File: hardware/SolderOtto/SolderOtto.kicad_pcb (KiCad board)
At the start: 4 copper layers, 121 x 60 mm, 221 parts, among them J201 Conn_02x04_Counter_Clockwise, J301 TC-2050, J401 Conn_01x20, J501 Conn_01x08, J601 Conn_01x07, P301 USB_C_Plug_USB2.0, Q201 T2N7002AK, Q202 BC858B, Q203 BC847A, Q204 BC847A, Q801 Q_Dual_NMOS, Q802 Q_Dual_NMOS, Q803 Q_Dual_NMOS, Q804 DTD123EK, Q805 DTD123EK, Q806 DTD123EK, Q807 Q_Dual_NMOS, Q808 Q_Dual_NMOS, Q809 DTD123EK, Q810 DTD123EK, Q901 BC847A, Q902 BC858B, Q903 BC847A, SW301 SW_Push, U201 LM5012, U202 AP3211K, U203 AP3211K, U204 AP3211K, U205 LM27761, U206 MCP9701T-E/TT, U301 USBLC6-2SC6, U302 STM32G474QETx, U303 MX25R3235FM1xx0, U701 SN74LVC125A, U702 TS5A3159ADCK, U801 VOM1271, U802 VOM1271, U803 VOM1271, U804 VOM1271, U805 VOM1271, U901 OP07, U902 LM358, U903 74hc4053, U904 OP07, U905 OP07, Y301 32.768 kHz

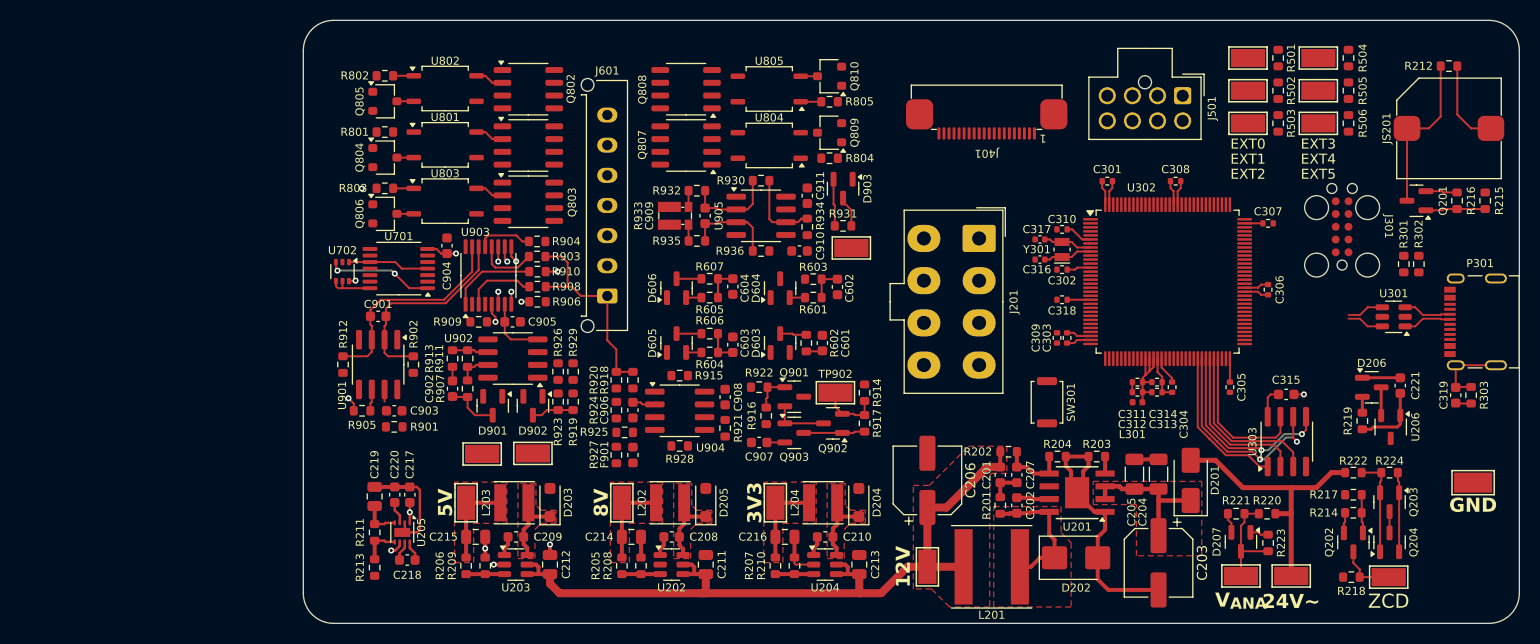
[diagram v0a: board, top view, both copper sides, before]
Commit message: try to replace op07c
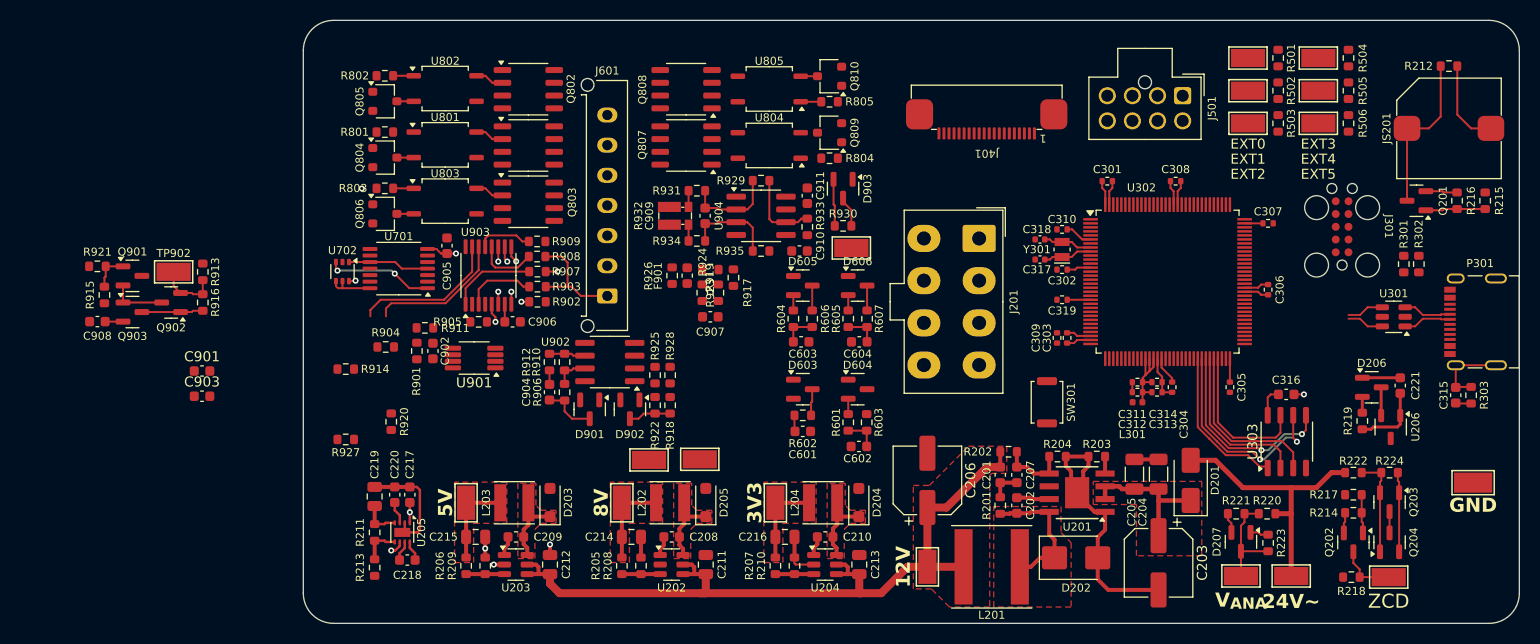
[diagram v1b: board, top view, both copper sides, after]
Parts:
- removed the C908 at (151.0, 87.5)
- removed the R901 at (118.0, 90.5)
- removed the U904 at (146.4, 88.8)
- added C901: 100n, Capacitor_SMD:C_0603_1608Metric, F.Cu at (98.9, 84.9)
- C903: value 1u -> 100n
- U303: footprint Package_SO:SOIC-8_3.9x4.9mm_P1.27mm -> Package_SO:SOP-8_3.9x4.9mm_P1.27mm
- U901: value OP07 -> OPA2206; footprint Package_SO:SOIC-8_3.9x4.9mm_P1.27mm -> Package_SO:VSSOP-8_3x3mm_P0.65mm
- moved C908 66.9 mm to (88.5, 80.0)
- moved R921 66.9 mm to (88.5, 74.5)
- moved Q901 66.9 mm to (92.0, 75.4)
- moved Q902 66.9 mm to (95.8, 78.1)
- moved Q903 66.9 mm to (92.0, 79.0)
- moved R913 66.9 mm to (99.0, 75.0)
- moved R915 66.9 mm to (89.2, 77.3)
- moved R916 66.9 mm to (99.0, 78.1)
- moved TP902 66.9 mm to (96.1, 75.0)
- moved R914 33.2 mm to (113.2, 84.7)
- moved R920 33.2 mm to (117.8, 89.9)
- moved R927 33.2 mm to (113.2, 91.7)
- moved C903 19.2 mm to (98.9, 87.4)
- moved R926 18.7 mm to (145.7, 75.4), turned to 90 degrees
- moved F901 18.6 mm to (147.2, 75.4), turned to 90 degrees
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- renumbered C319 to C315, C315 to C316, C316 to C317, C317 to C318, C318 to C319, C901 to C902, C902 to C904, C904 to C905, C905 to C906, C906 to C907, C907 to C908, R902 to R901, R906 to R902, R908 to R903, R905 to R904, R909 to R905, R907 to R906, R910 to R907, R903 to R908, R904 to R909, R911 to R910, R912 to R911, R913 to R912, R914 to R913, R915 to R914, R916 to R915, R917 to R916, R918 to R917, R919 to R918, R920 to R919, R921 to R920, R922 to R921, R923 to R922, R924 to R923, R925 to R924, R926 to R925, R927 to R926, R928 to R927, R929 to R928, R930 to R929, R931 to R930, R932 to R931, R933 to R932, R934 to R933, R935 to R934, R936 to R935, U905 to U904
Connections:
- C902 pad 2: Net-(U901-+) -> Net-(U901B-+)
- C903 pad 1: +8V -> -5V
- C907 pad 1: Net-(U904--) (its old number) -> Net-(U901A--)
- C907 pad 2: Net-(U904-+) (its old number) -> Net-(U901A-+)
- R901 pad 2: Net-(R902-Pad2) -> Net-(R901-Pad2)
- R904 pad 1: Net-(R902-Pad2) -> Net-(R901-Pad2)
- R911 pad 1: Net-(U901-+) -> Net-(U901B-+)
- R914 pad 1: Net-(U904--) (its old number) -> Net-(U901A--)
- R914 pad 2: Net-(R915-Pad2) -> Net-(R914-Pad2)
- R917 pad 2: Net-(U904--) (its old number) -> Net-(U901A--)
- R920 pad 1: Net-(R915-Pad2) -> Net-(R914-Pad2)
- R924 pad 1: Net-(U904-+) (its old number) -> Net-(U901A-+)
- R927 pad 1: Net-(U904-+) (its old number) -> Net-(U901A-+)
- U901 pad 1: unconnected-(U901-VOS-Pad1) -> Net-(R914-Pad2)
- U901 pad 2: /Channel0/channel_meas/IN- -> Net-(U901A--)
- U901 pad 3: Net-(U901-+) -> Net-(U901A-+)
- U901 pad 5: unconnected-(U901-NC-Pad5) -> Net-(U901B-+)
- U901 pad 6: Net-(R902-Pad2) -> /Channel0/channel_meas/IN-
- U901 pad 7: +8V -> Net-(R901-Pad2)
- U901 pad 8: Net-(R901-Pad2) -> +8V
- U903 pad 15: Net-(U901-+) -> Net-(U901B-+)
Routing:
- net Net-(U901-+): track 22.3 -> 0.00 mm
- net Net-(U901B-+): track 0.00 -> 15.7 mm
- net /Channel0/TC: track 20.9 -> 11.4 mm
- net /Channel0/channel_meas/IN-: track 20.6 -> 13.9 mm
- net -5V: track 10.3 -> 5.60 mm
- net Net-(U904--) (its old number): track 2.26 -> 0.00 mm
- net Net-(R902-Pad2): track 2.18 -> 0.00 mm
- net Net-(U902B-+): track 1.47 -> 0.00 mm, vias 1 -> 0
- net +8V: track 10.1 -> 8.85 mm

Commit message: save work
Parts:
- removed C911: 1u, Capacitor_SMD:C_0603_1608Metric
- removed U904: OP07, Package_SO:SOIC-8_3.9x4.9mm_P1.27mm
- added C912: 100n, Capacitor_SMD:C_0603_1608Metric, F.Cu at (128.0, 87.6)
- added C913: 100n, Capacitor_SMD:C_0603_1608Metric, F.Cu at (154.4, 66.8)
- added U905: OPA206, Package_SO:VSSOP-8_3x3mm_P0.65mm, F.Cu at (153.4, 69.5)
- U902: value LM358 -> LM358B; footprint Package_SO:SOIC-8_3.9x4.9mm_P1.27mm -> Package_SO:VSSOP-8_3x3mm_P0.65mm
- moved R917 62.5 mm to (88.6, 87.2)
- moved R919 62.5 mm to (90.1, 85.7)
- moved C907 62.5 mm to (87.8, 89.6)
- moved R923 62.5 mm to (87.8, 84.9)
- moved R924 62.5 mm to (87.0, 87.2)
- moved F901 62.5 mm to (85.5, 85.5)
- moved R926 62.5 mm to (84.0, 85.5)
- moved C903 57.6 mm to (154.4, 72.1)
- moved TP901 55.8 mm to (88.2, 101.6)
- moved TP903 49.1 mm to (100.0, 101.6)
- moved C904 46.8 mm to (88.0, 98.0)
- moved R906 46.8 mm to (89.5, 98.0)
- moved R910 46.8 mm to (89.5, 95.0)
- moved R912 46.8 mm to (88.0, 95.0)
- moved U902 46.8 mm to (94.0, 95.0)
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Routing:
- net Net-(U905-+): track 9.07 -> 0.00 mm
- net Net-(U905--): track 9.07 -> 0.00 mm
- net Net-(R929-Pad2): track 7.88 -> 0.00 mm
- net +3V3: track 53.4 -> 48.7 mm
- net Net-(U902A--): track 0.00 -> 4.09 mm
- net Net-(R922-Pad2): track 0.00 -> 3.94 mm
- net /Channel0/T_{TIP}: track 5.40 -> 1.52 mm
- net /Channel0/I_{LOAD}: track 3.10 -> 0.00 mm
- net Net-(R932-Pad3): track 1.62 -> 0.00 mm
- net Net-(R931-Pad1): track 1.61 -> 0.00 mm
- net Net-(U902B--): track 3.60 -> 2.59 mm

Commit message: save work
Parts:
- removed the R919 at (90.1, 85.7)
- added C904: 100n, Capacitor_SMD:C_0603_1608Metric, F.Cu at (120.8, 87.2)
- added C907: 100n, Capacitor_SMD:C_0603_1608Metric, F.Cu at (103.5, 92.3)
- added C910: 1n, Capacitor_SMD:C_0603_1608Metric, F.Cu at (104.5, 82.5)
- added U904: OPA202, Package_SO:VSSOP-8_3x3mm_P0.65mm, F.Cu at (102.0, 95.0)
- R923: value 220m -> 400m; footprint Resistor_SMD:R_0603_1608Metric -> Resistor_SMD:R_1206_3216Metric
- U901: value OPA2206 -> OPA202
- U905: value OPA206 -> OPA202
- moved TP903 46.4 mm to (145.2, 91.3)
- moved R919 46.3 mm to (145.2, 88.4)
- moved R922 46.3 mm to (143.7, 88.4)
- moved R925 46.3 mm to (143.7, 85.4)
- moved R928 46.3 mm to (145.2, 85.4)
- moved D901 46.2 mm to (137.3, 89.1)
- moved D902 46.2 mm to (141.1, 89.1)
- moved C903 46.2 mm to (133.2, 88.4)
- moved R906 46.2 mm to (134.7, 88.4)
- moved R910 46.2 mm to (134.7, 85.4)
- moved R912 46.2 mm to (133.2, 85.4)
- moved U902 46.2 mm to (139.2, 85.4)
- moved TP901 46.2 mm to (133.2, 91.3)
- moved C911 27.2 mm to (102.8, 97.7), turned to 0 degrees
- moved C901 26.6 mm to (124.7, 91.3)
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- renumbered C904 to C903, C907 to C909, C912 to C911, C913 to C912, C909 to C913, C910 to C914, C903 to C915, R915 to R914, R916 to R915, R914 to R916, R921 to R918, R918 to R919, R920 to R921
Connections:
- C902 pad 2: Net-(U901B-+) -> Net-(U901A-+)
- C909 pad 1: Net-(U901A--) -> Net-(U904A--)
- C909 pad 2: Net-(U901A-+) -> Net-(U904A-+)
- R911 pad 1: Net-(U901B-+) -> Net-(U901A-+)
- R916 pad 1: Net-(U901A--) -> Net-(U904A--)
- R916 pad 2: Net-(R914-Pad2) -> Net-(R916-Pad2)
- R917 pad 2: Net-(U901A--) -> Net-(U904A--)
- R921 pad 1: Net-(R914-Pad2) -> Net-(R916-Pad2)
- R923 pad 1: Net-(R919-Pad2) -> /Channel0/TC
- R924 pad 1: Net-(U901A-+) -> Net-(U904A-+)
- R927 pad 1: Net-(U901A-+) -> Net-(U904A-+)
- U901 pad 1: Net-(R914-Pad2) -> unconnected-(U901A-NC-Pad1)
- U901 pad 2: Net-(U901A--) -> /Channel0/channel_meas/IN-
- U901 pad 5: Net-(U901B-+) -> unconnected-(U901A-NC-Pad5)
- U901 pad 6: /Channel0/channel_meas/IN- -> Net-(R901-Pad2)
- U901 pad 7: Net-(R901-Pad2) -> +8V
- U901 pad 8: +8V -> unconnected-(U901A-NC-Pad8)
- U903 pad 15: Net-(U901B-+) -> Net-(U901A-+)
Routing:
- net Net-(U901B-+): track 15.7 -> 0.00 mm
- net /Channel0/channel_meas/IN-: track 13.9 -> 4.11 mm
- net Net-(R929-Pad2): track 0.00 -> 9.41 mm
- net Net-(U903-2Y1): track 8.61 -> 0.00 mm
- net /Channel0/I_{LOAD}: track 0.00 -> 8.11 mm
- net Net-(U903-3Y1): track 7.13 -> 0.00 mm
- net Net-(U903-1Y0): track 6.02 -> 0.00 mm
- net Net-(R901-Pad2): track 0.00 -> 5.89 mm
- net Net-(U903-1Y1): track 5.54 -> 0.00 mm
- net GND: track 94.8 -> 89.2 mm, vias 7 -> 4
- net Net-(U905A-+): track 0.00 -> 5.51 mm
- net Net-(U905A--): track 0.00 -> 5.46 mm
- net /Channel0/T_{TIP}: track 1.52 -> 6.58 mm
- net Net-(U901A-+): track 0.00 -> 4.11 mm
- net Net-(U902A-+): track 0.00 -> 3.81 mm
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
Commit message: save work
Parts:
- added R919: 220m, Resistor_SMD:R_0805_2012Metric, F.Cu at (148.9, 75.7)
- R923: value 400m -> 220m; footprint Resistor_SMD:R_1206_3216Metric -> Resistor_SMD:R_0805_2012Metric
- moved R917 59.6 mm to (153.3, 75.8), turned to 0 degrees
- moved R916 57.2 mm to (154.2, 78.3), turned to -90 degrees
- moved C909 56.5 mm to (151.6, 77.5), turned to 180 degrees
- moved R924 55.2 mm to (148.1, 77.5), turned to 180 degrees
- moved R926 54.9 mm to (145.9, 78.3)
- moved R923 54.4 mm to (145.3, 75.7), turned to 180 degrees
- moved F901 52.2 mm to (144.4, 78.2)
- moved C907 51.6 mm to (154.2, 83.2), turned to -90 degrees
- moved U904 51.4 mm to (151.6, 81.5), turned to -90 degrees
- moved C911 48.9 mm to (148.9, 81.5), turned to -90 degrees
- moved C910 39.2 mm to (143.3, 87.8), turned to 90 degrees
- moved R927 36.0 mm to (148.1, 79.0), turned to 180 degrees
- moved C908 30.3 mm to (116.9, 90.5), turned to -90 degrees
- moved R914 28.0 mm to (114.2, 89.8), turned to 180 degrees
- moved R918 28.0 mm to (111.4, 90.5), turned to 90 degrees
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- renumbered R919 to R920
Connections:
- R923 pad 1: /Channel0/TC -> Net-(R919-Pad2)
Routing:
- net /Channel0/channel_meas/IN-: track 4.11 -> 16.6 mm
- net Net-(U901A-+): track 4.11 -> 16.6 mm
- net /Channel0/TC: track 11.4 -> 0.00 mm
- net +8V: track 12.4 -> 15.9 mm
- net -5V: track 8.12 -> 11.0 mm
- net Net-(R901-Pad2): track 5.89 -> 7.95 mm
- net Net-(U902A--): track 2.86 -> 4.36 mm
- net GND: track 89.2 -> 90.6 mm
- net /Channel0/LOAD: track 1.18 -> 0.00 mm, vias 1 -> 0
- net /Channel0/I_{LEAK}: track 6.51 -> 5.98 mm
- net Net-(U903-3Y0): vias 1 -> 0

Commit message: save work
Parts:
- moved D605 14.3 mm to (144.8, 79.8), turned to 90 degrees
- moved C602 13.7 mm to (160.7, 75.2)
- moved D604 13.7 mm to (155.0, 75.3)
- moved R601 13.7 mm to (158.3, 76.2)
- moved R603 13.7 mm to (158.3, 74.4)
- moved C601 13.6 mm to (149.0, 75.4)
- moved D603 13.6 mm to (144.8, 75.4)
- moved R602 13.6 mm to (147.4, 75.4)
- moved R606 11.6 mm to (148.1, 78.9), turned to 0 degrees
- moved R916 10.2 mm to (160.3, 86.4)
- moved R926 10.2 mm to (152.1, 86.4)
- moved R927 10.2 mm to (154.3, 87.2)
- moved C907 10.2 mm to (160.4, 91.3)
- moved C909 10.2 mm to (157.8, 85.6)
- moved F901 10.2 mm to (150.6, 86.3)
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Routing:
- net Net-(U901A-+): track 16.6 -> 11.8 mm
- net /Channel0/channel_meas/IN-: track 16.6 -> 11.8 mm
- net Net-(R901-Pad2): track 7.95 -> 7.05 mm

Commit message: save work
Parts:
- moved J501 5.48 mm to (192.5, 53.8), turned to 0 degrees
- moved J201 2.30 mm to (176.2, 74.0)
- moved TP501 2.06 mm to (201.0, 54.2)
- moved TP502 2.06 mm to (201.0, 57.5)
- moved TP503 2.06 mm to (201.0, 60.8)
- moved TP504 2.06 mm to (208.0, 54.2)
- moved TP505 2.06 mm to (208.0, 57.5)
- moved TP506 2.06 mm to (208.0, 60.8)
- moved R501 2.03 mm to (204.0, 53.4)
- moved R502 2.03 mm to (204.0, 56.7)
- moved R503 2.03 mm to (204.0, 59.9)
- moved R504 2.03 mm to (211.0, 53.4)
- moved R505 2.03 mm to (211.0, 56.7)
- moved R506 2.03 mm to (211.0, 59.9)
- moved J301 1.22 mm to (212.6, 75.5)
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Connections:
- J501 pad 2: /External connection/EXT_0 -> /External connection/EXT_5
- J501 pad 3: /External connection/EXT_1 -> /External connection/EXT_4
- J501 pad 4: /External connection/EXT_2 -> /External connection/EXT_3
- J501 pad 6: /External connection/EXT_3 -> /External connection/EXT_2
- J501 pad 7: /External connection/EXT_4 -> /External connection/EXT_1
- J501 pad 8: /External connection/EXT_5 -> /External connection/EXT_0
- R501 pad 2: /External connection/EXT_0 -> /External connection/EXT_5
- R502 pad 2: /External connection/EXT_1 -> /External connection/EXT_4
- R503 pad 2: /External connection/EXT_2 -> /External connection/EXT_3
- R504 pad 2: /External connection/EXT_3 -> /External connection/EXT_2
- R505 pad 2: /External connection/EXT_4 -> /External connection/EXT_1
- R506 pad 2: /External connection/EXT_5 -> /External connection/EXT_0
- TP501 pad 1: /External connection/EXT_0 -> /External connection/EXT_5
- TP502 pad 1: /External connection/EXT_1 -> /External connection/EXT_4
- TP503 pad 1: /External connection/EXT_2 -> /External connection/EXT_3
- TP504 pad 1: /External connection/EXT_3 -> /External connection/EXT_2
- TP505 pad 1: /External connection/EXT_4 -> /External connection/EXT_1
- TP506 pad 1: /External connection/EXT_5 -> /External connection/EXT_0
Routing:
- net 24V_{AC}: track 27.5 -> 125.5 mm
- net +3V3: track 48.7 -> 105.4 mm
- net /External connection/EXT_2: track 0.00 -> 38.3 mm, vias 0 -> 2
- net /Channel0/COM: track 0.00 -> 35.9 mm, vias 0 -> 15
- net /External connection/EXT_1: track 0.00 -> 32.9 mm, vias 0 -> 2
- net /Channel0/LOAD: track 0.00 -> 31.5 mm, vias 0 -> 15
- net /External connection/EXT_0: track 0.00 -> 29.5 mm, vias 0 -> 2
- net /External connection/EXT_5: track 0.00 -> 27.6 mm
- net /External connection/EXT_4: track 0.00 -> 23.1 mm
- net /Display/~{INT}: track 0.00 -> 21.1 mm, vias 0 -> 2
- net /External connection/EXT_3: track 0.00 -> 20.0 mm
- net /Display/SPI_MOSI: track 0.00 -> 19.9 mm, vias 0 -> 2
- net /Display/SPI_MISO: track 0.00 -> 19.7 mm, vias 0 -> 2
- net /Channel0/channel_meas/CURRENT: track 0.00 -> 18.3 mm, vias 0 -> 18
- net /Display/QSPI_CS: track 0.00 -> 17.8 mm, vias 0 -> 2
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- added copper zone on B.Cu, net /Channel0/COM
- added copper zone on F.Cu, net /Channel0/COM
- added copper zone on In1.Cu, net /Channel0/COM
- added copper zone on In2.Cu, net /Channel0/COM
- added copper zone on B.Cu, net /Channel0/LOAD
- added copper zone on F.Cu, net /Channel0/LOAD
- added copper zone on In1.Cu, net /Channel0/LOAD
- added copper zone on In2.Cu, net /Channel0/LOAD
- added copper zone on B.Cu, net /Channel0/_iron_sense
- added copper zone on F.Cu, net /Channel0/_iron_sense
- added copper zone on In1.Cu, net /Channel0/_iron_sense
- added copper zone on In2.Cu, net /Channel0/_iron_sense
- added copper zone on B.Cu, net /Channel0/channel_meas/CURRENT
- added copper zone on F.Cu, net /Channel0/channel_meas/CURRENT
- added copper zone on In1.Cu, net /Channel0/channel_meas/CURRENT
- added copper zone on In2.Cu, net /Channel0/channel_meas/CURRENT
- added copper zone on B.Cu, net 24V_{AC}
- added copper zone on F.Cu, net 24V_{AC}
- added copper zone on In1.Cu, net GND
- added copper zone on B.Cu, net Net-(Q801A-S)
- added copper zone on F.Cu, net Net-(Q801A-S)
- added copper zone on In1.Cu, net Net-(Q801A-S)
- added copper zone on In2.Cu, net Net-(Q801A-S)
- added copper zone on B.Cu, net Net-(Q802A-S)
- added copper zone on F.Cu, net Net-(Q802A-S)
- added copper zone on In1.Cu, net Net-(Q802A-S)
- added copper zone on In2.Cu, net Net-(Q802A-S)
- added copper zone on B.Cu, net Net-(Q803A-S)
- added copper zone on F.Cu, net Net-(Q803A-S)
- added copper zone on In1.Cu, net Net-(Q803A-S)
- added copper zone on In2.Cu, net Net-(Q803A-S)
- added copper zone on B.Cu, net Net-(Q807A-S)
- added copper zone on F.Cu, net Net-(Q807A-S)
- added copper zone on In1.Cu, net Net-(Q807A-S)
- added copper zone on In2.Cu, net Net-(Q807A-S)
- added copper zone on B.Cu, net Net-(Q808A-S)
- added copper zone on F.Cu, net Net-(Q808A-S)
- added copper zone on In1.Cu, net Net-(Q808A-S)
- added copper zone on In2.Cu, net Net-(Q808A-S)
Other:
- board size 121 x 60 mm -> 120 x 60 mm

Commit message: layout finished
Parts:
- added C701: 100n, Capacitor_SMD:C_0603_1608Metric, F.Cu at (167.6, 69.8)
- added C702: 100n, Capacitor_SMD:C_0603_1608Metric, F.Cu at (120.7, 71.4)
- moved U702 55.8 mm to (167.4, 67.6), turned to 0 degrees
- moved D603 18.2 mm to (162.3, 80.3), turned to -90 degrees
- moved D605 17.9 mm to (162.3, 75.9), turned to -90 degrees
- moved C602 15.2 mm to (146.4, 80.5), turned to 90 degrees
- moved C604 14.6 mm to (146.4, 76.1), turned to 90 degrees
- moved R602 13.0 mm to (159.0, 81.2), turned to 180 degrees
- moved R604 12.3 mm to (159.0, 75.0), turned to 180 degrees
- moved R603 11.8 mm to (148.7, 81.2), turned to 180 degrees
- moved R605 11.2 mm to (148.7, 75.0), turned to 180 degrees
- moved R606 11.1 mm to (159.0, 76.8), turned to 180 degrees
- moved C601 10.7 mm to (158.9, 79.4), turned to 0 degrees
- moved R601 10.1 mm to (148.7, 79.4), turned to 180 degrees
- moved R607 9.81 mm to (148.7, 76.8), turned to 180 degrees
- moved C603 7.59 mm to (156.7, 75.7), turned to -90 degrees
- moved D604 5.83 mm to (152.0, 80.3), turned to -90 degrees
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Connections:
- U302 pad 22: /Channel0/handle_id -> /Channel0/I_{LOAD}
- U302 pad 23: /Channel0/T_{TIP} -> /Channel0/handle_id
- U302 pad 24: /Channel0/I_{LEAK} -> /Channel0/T_{TIP}
- U302 pad 25: /Channel0/I_{LOAD} -> /Channel0/I_{LEAK}
- U302 pad 27: /Channel0/LOAD0_SW -> /Channel0/COM_SW
- U302 pad 28: /Channel0/LOAD1_SW -> /Channel0/LOAD0_SW
- U302 pad 29: /Channel0/COM_SW -> /Channel0/LOAD1_SW
- U701 pad 1: /Channel0/channel_power/COM_SW_LOW -> unconnected-(U701A-~{OE}-Pad1)
- U701 pad 11: unconnected-(U701D-Y-Pad11) -> /Channel0/channel_power/COM_SW_HIGH
- U701 pad 12: unconnected-(U701D-A-Pad12) -> /Channel0/COM_SW
- U701 pad 13: unconnected-(U701D-~{OE}-Pad13) -> /Channel0/channel_power/COM_SW_LOW
- U701 pad 2: /Channel0/COM_SW -> unconnected-(U701A-A-Pad2)
- U701 pad 3: /Channel0/channel_power/COM_SW_HIGH -> unconnected-(U701A-Y-Pad3)
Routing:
- net GND: track 93.6 -> 824.0 mm, vias 13 -> 84
- net +3V3: track 105.4 -> 439.8 mm, vias 0 -> 28
- net +5V: track 25.7 -> 214.8 mm, vias 2 -> 6
- net +12V: track 77.0 -> 217.8 mm, vias 0 -> 6
- net /Channel0/DET: track 9.38 -> 112.1 mm, vias 0 -> 2
- net +8V: track 15.9 -> 97.9 mm, vias 0 -> 4
- net -5V: track 11.0 -> 87.7 mm, vias 0 -> 6
- net /Channel0/LOAD0_SW: track 0.00 -> 75.8 mm, vias 0 -> 2
- net Earth: track 1.55 -> 76.2 mm, vias 0 -> 2
- net /Channel0/LOAD1_SW: track 0.00 -> 72.4 mm, vias 0 -> 2
- net /Channel0/COM_SW: track 0.00 -> 70.1 mm, vias 0 -> 2
- net /Channel0/TC: track 0.00 -> 69.7 mm, vias 0 -> 3
- net /Channel0/SEL3: track 0.00 -> 65.4 mm, vias 0 -> 2
- net /Channel0/SEL2: track 0.00 -> 64.1 mm, vias 0 -> 2
- net /Channel0/channel_power/LOAD_SW_LOW: track 0.00 -> 63.8 mm, vias 0 -> 2
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- added copper zone on F.Cu, net -5V
- added copper zone on B.Cu, net GND
- added copper zone on F.Cu, net GND
- removed copper zone on In1.Cu, net /Channel0/COM
- removed copper zone on In2.Cu, net /Channel0/COM
- removed copper zone on In1.Cu, net /Channel0/LOAD
- removed copper zone on In2.Cu, net /Channel0/LOAD
- removed copper zone on In1.Cu, net /Channel0/_iron_sense
- removed copper zone on In2.Cu, net /Channel0/_iron_sense
- removed copper zone on In1.Cu, net /Channel0/channel_meas/CURRENT
- removed copper zone on In2.Cu, net /Channel0/channel_meas/CURRENT
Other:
- board text added: "1"
